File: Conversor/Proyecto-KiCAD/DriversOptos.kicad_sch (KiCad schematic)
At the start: 29 parts, among them U10 ACPL-P480, U11 2ED21834-S06J, U12 2ED21834-S06J, U7 ACPL-P480, U8 ACPL-P480, U9 ACPL-P480

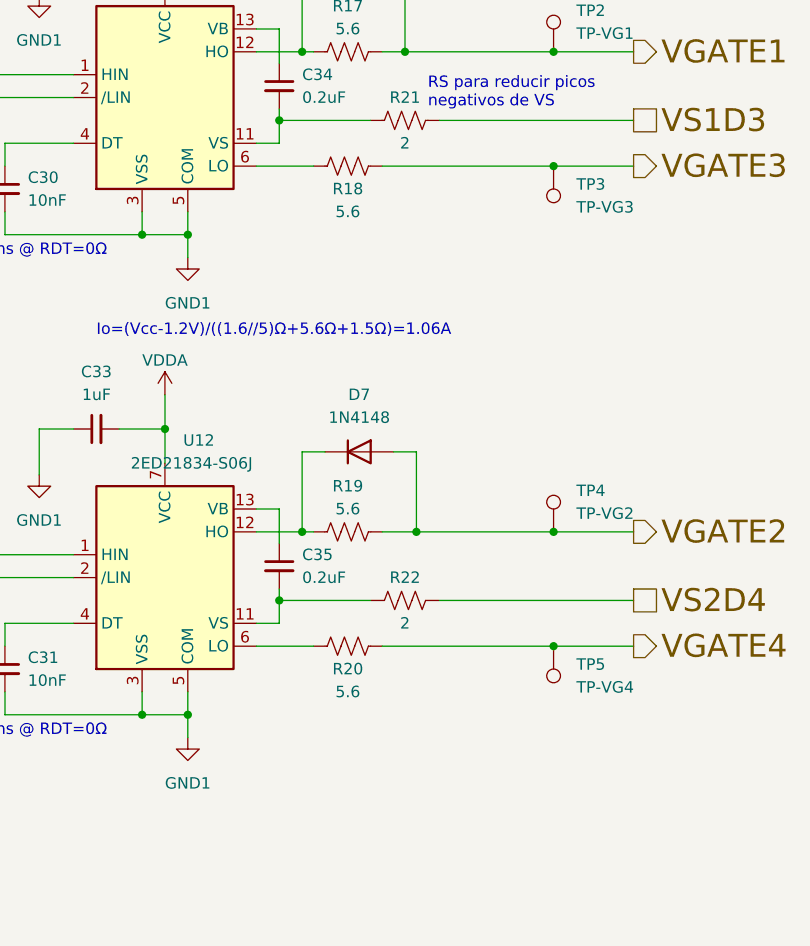
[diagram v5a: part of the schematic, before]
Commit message: Arreglar los primeros dos items marcados por Jorge
- Usar EPWM1A/B y EPWM2A/B para poder usar la función de phase-shift de
los modulos PWM y ahorrarse la sincronización manual
- Agregar diodos de descarga D8 y D9 a la salida de los drivers
- Agregar el Technical Reference Manual del DSP a la bibliografía
(descripción ultra detallada de todas las funciones del DSP)
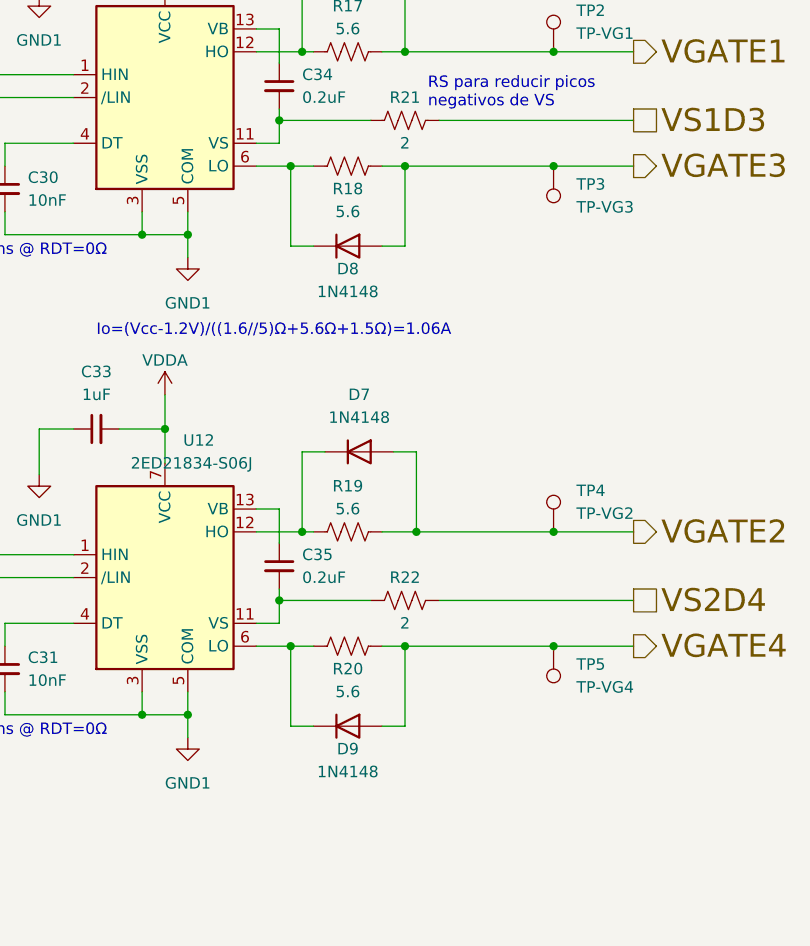
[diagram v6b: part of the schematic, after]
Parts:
- added D8, D9: 1N4148, Diode_THT:D_DO-35_SOD27_P7.62mm_Horizontal, symbol Diode:1N4148
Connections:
- net VGATE3: now also D8.2 (A)
- net VGATE4: now also D9.2 (A)
- net at R20.1, U12.6 (LO): now also D9.1 (K)
- net at R18.1, U11.6 (LO): now also D8.1 (K)
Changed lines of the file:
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@@
 (kicad_sch (version 20211123) (generator eeschema)
   (paper "A4")
+  (junction (at 205.74 129.54) (diameter 0) (color 0 0 0 0)
+  )
   (junction (at 219.71 116.84) (diameter 0) (color 0 0 0 0)
   )
@@
   (junction (at 144.78 46.99) (diameter 0) (color 0 0 0 0)
   )
+  (junction (at 218.44 129.54) (diameter 0) (color 0 0 0 0)
+  )
   (junction (at 234.95 63.5) (diameter 0) (color 0 0 0 0)
   )
+  (junction (at 218.44 76.2) (diameter 0) (color 0 0 0 0)
+  )
   (junction (at 234.95 76.2) (diameter 0) (color 0 0 0 0)
   )
@@
   (junction (at 234.95 116.84) (diameter 0) (color 0 0 0 0)
   )
+  (junction (at 205.74 76.2) (diameter 0) (color 0 0 0 0)
+  )
   (junction (at 144.78 106.68) (diameter 0) (color 0 0 0 0)
   )
@@
     (stroke (width 0) (type default) (color 0 0 0 0))
   )
+  (wire (pts (xy 218.44 129.54) (xy 218.44 138.43))
+    (stroke (width 0) (type default) (color 0 0 0 0))
+  )
   (wire (pts (xy 144.78 67.31) (xy 147.32 67.31))
     (stroke (width 0) (type default) (color 0 0 0 0))
@@
     (stroke (width 0) (type default) (color 0 0 0 0))
   )
-  (wire (pts (xy 201.93 129.54) (xy 208.28 129.54))
+  (wire (pts (xy 201.93 129.54) (xy 205.74 129.54))
     (stroke (width 0) (type default) (color 0 0 0 0))
   )
@@
     (stroke (width 0) (type default) (color 0 0 0 0))
   )
-  (wire (pts (xy 215.9 129.54) (xy 234.95 129.54))
+  (wire (pts (xy 215.9 129.54) (xy 218.44 129.54))
     (stroke (width 0) (type default) (color 0 0 0 0))
   )
@@
     (stroke (width 0) (type default) (color 0 0 0 0))
   )
+  (wire (pts (xy 215.9 85.09) (xy 218.44 85.09))
+    (stroke (width 0) (type default) (color 0 0 0 0))
+  )
   (wire (pts (xy 181.61 127) (xy 173.99 127))
     (stroke (width 0) (type default) (color 0 0 0 0))
@@
     (stroke (width 0) (type default) (color 0 0 0 0))
   )
+  (wire (pts (xy 205.74 129.54) (xy 205.74 138.43))
+    (stroke (width 0) (type default) (color 0 0 0 0))
+  )
   (wire (pts (xy 201.93 116.84) (xy 207.01 116.84))
     (stroke (width 0) (type default) (color 0 0 0 0))
@@
     (stroke (width 0) (type default) (color 0 0 0 0))
   )
+  (wire (pts (xy 205.74 76.2) (xy 205.74 85.09))
+    (stroke (width 0) (type default) (color 0 0 0 0))
+  )
   (wire (pts (xy 144.78 46.99) (xy 147.32 46.99))
     (stroke (width 0) (type default) (color 0 0 0 0))
@@
     (stroke (width 0) (type default) (color 0 0 0 0))
   )
-  (wire (pts (xy 215.9 76.2) (xy 234.95 76.2))
+  (wire (pts (xy 215.9 76.2) (xy 218.44 76.2))
     (stroke (width 0) (type default) (color 0 0 0 0))
   )
@@
     (stroke (width 0) (type default) (color 0 0 0 0))
   )
+  (wire (pts (xy 205.74 76.2) (xy 208.28 76.2))
+    (stroke (width 0) (type default) (color 0 0 0 0))
+  )
+  (wire (pts (xy 218.44 85.09) (xy 218.44 76.2))
+    (stroke (width 0) (type default) (color 0 0 0 0))
+  )
   (wire (pts (xy 181.61 52.07) (xy 177.8 52.07))
     (stroke (width 0) (type default) (color 0 0 0 0))
@@
   )
   (wire (pts (xy 55.88 90.17) (xy 64.77 90.17))
+    (stroke (width 0) (type default) (color 0 0 0 0))
+  )
+  (wire (pts (xy 205.74 129.54) (xy 208.28 129.54))
+    (stroke (width 0) (type default) (color 0 0 0 0))
+  )
+  (wire (pts (xy 208.28 85.09) (xy 205.74 85.09))
+    (stroke (width 0) (type default) (color 0 0 0 0))
+  )
+  (wire (pts (xy 218.44 129.54) (xy 234.95 129.54))
+    (stroke (width 0) (type default) (color 0 0 0 0))
+  )
+  (wire (pts (xy 208.28 138.43) (xy 205.74 138.43))
     (stroke (width 0) (type default) (color 0 0 0 0))
   )
@@
     (stroke (width 0) (type default) (color 0 0 0 0))
   )
+  (wire (pts (xy 218.44 76.2) (xy 234.95 76.2))
+    (stroke (width 0) (type default) (color 0 0 0 0))
+  )
   (wire (pts (xy 113.03 78.74) (xy 113.03 80.01))
     (stroke (width 0) (type default) (color 0 0 0 0))
@@
     (stroke (width 0) (type default) (color 0 0 0 0))
   )
+  (wire (pts (xy 215.9 138.43) (xy 218.44 138.43))
+    (stroke (width 0) (type default) (color 0 0 0 0))
+  )
   (wire (pts (xy 162.56 114.3) (xy 162.56 119.38))
     (stroke (width 0) (type default) (color 0 0 0 0))
@@
     (stroke (width 0) (type default) (color 0 0 0 0))
   )
-  (wire (pts (xy 201.93 76.2) (xy 208.28 76.2))
+  (wire (pts (xy 201.93 76.2) (xy 205.74 76.2))
     (stroke (width 0) (type default) (color 0 0 0 0))
   )
@@
     (pin "1")
   )
+  (symbol (lib_id "Diode:1N4148") (at 212.09 138.43 0) (unit 1)
+    (in_bom yes) (on_board yes)
+    (property "Reference" "D9" (id 0) (at 212.09 140.97 0))
+    (property "Value" "1N4148" (id 1) (at 212.09 143.51 0))
+    (property "Footprint" "Diode_THT:D_DO-35_SOD27_P7.62mm_Horizontal" (id 2) (at 212.09 142.875 0)
+      (effects (font (size 1.27 1.27)) hide)
+    )
+    (property "Datasheet" "https://assets.nexperia.com/documents/data-sheet/1N4148_1N4448.pdf" (id 3) (at 212.09 138.43 0)
+      (effects (font (size 1.27 1.27)) hide)
+    )
+    (pin "1")
+    (pin "2")
+  )
+  (symbol (lib_id "Diode:1N4148") (at 212.09 85.09 0) (unit 1)
+    (in_bom yes) (on_board yes)
+    (property "Reference" "D8" (id 0) (at 212.09 87.63 0))
+    (property "Value" "1N4148" (id 1) (at 212.09 90.17 0))
+    (property "Footprint" "Diode_THT:D_DO-35_SOD27_P7.62mm_Horizontal" (id 2) (at 212.09 89.535 0)
+      (effects (font (size 1.27 1.27)) hide)
+    )
+    (property "Datasheet" "https://assets.nexperia.com/documents/data-sheet/1N4148_1N4448.pdf" (id 3) (at 212.09 85.09 0)
+      (effects (font (size 1.27 1.27)) hide)
+    )
+    (pin "1")
+    (pin "2")
+  )
 )

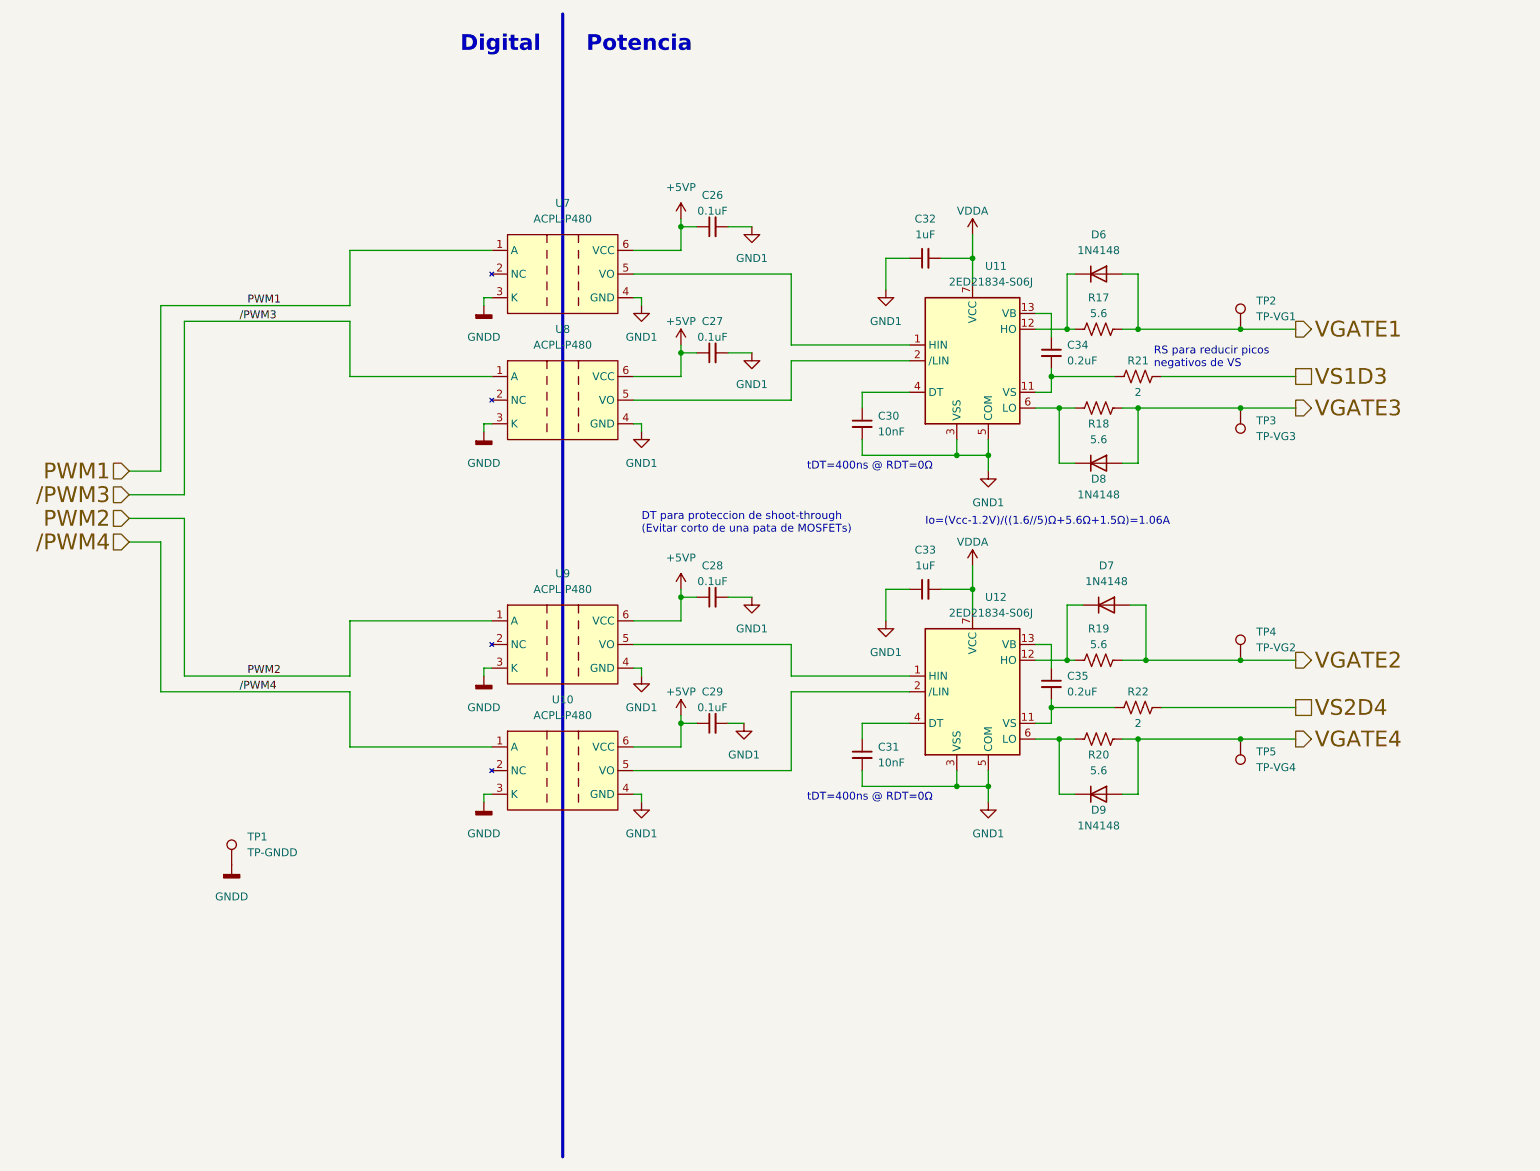
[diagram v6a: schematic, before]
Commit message: Terminar el resto de los cambios de Jorge
- Capacitores electroliticos para el circuito de bootstrap, en paralelo
a los cerámicos
- Cambiar el I2C a 3V3 del lado digital
- Hacer la separacion de linea de datos de I2C del lado digital como en
la nota de aplicación SLYT403A
- Dejar el Vaux del LM5056A con un jumper por si acaso
- Lo mismo con la resistencia de dead-time RDT de los drivers, dejar una
footprint de resistencia SMD para poder cambiarlas de ser necesario
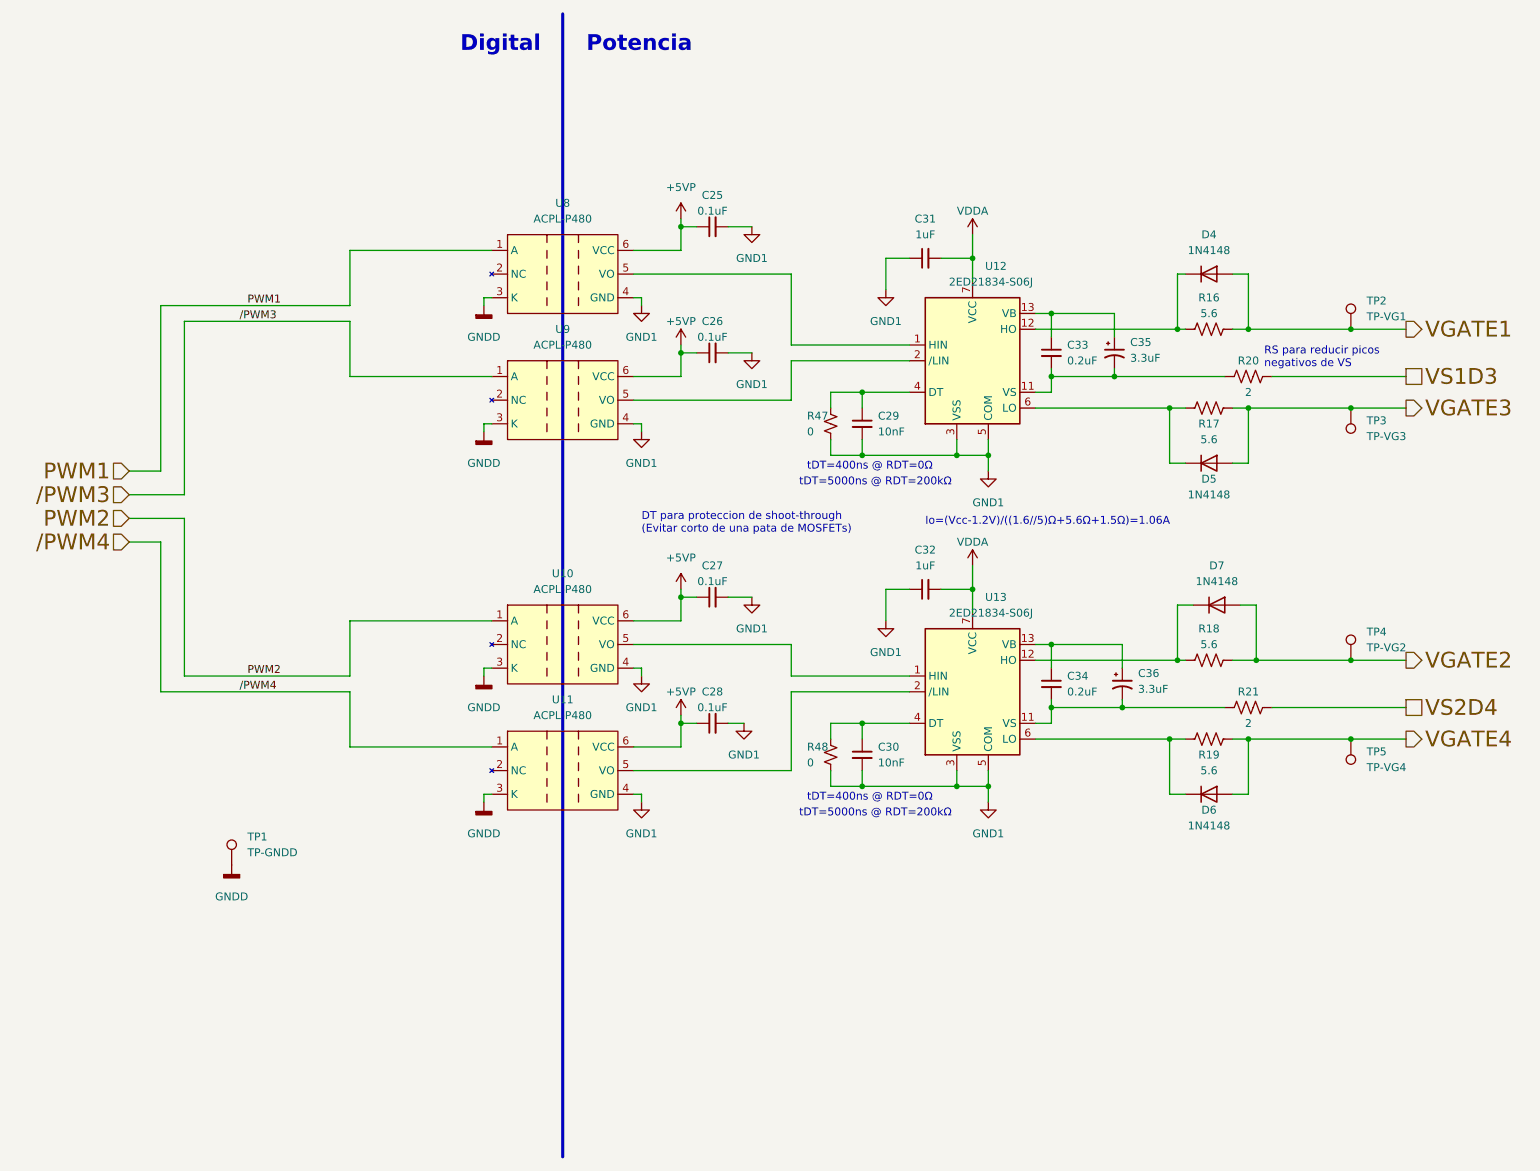
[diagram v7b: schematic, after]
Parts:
- added C35, C36: 3.3uF, Capacitor_THT:CP_Radial_D4.0mm_P2.00mm, symbol Device:C_Polarized_Small_US
- added R47, R48: 0, Resistor_SMD:R_1206_3216Metric_Pad1.30x1.75mm_HandSolder, symbol Device:R_Small_US
- renumbered C26 to C25, C27 to C26, C28 to C27, C29 to C28, C30 to C29, C31 to C30, C32 to C31, C33 to C32, C34 to C33, C35 to C34, D6 to D4, D8 to D5, D9 to D6, R17 to R16, R18 to R17, R19 to R18, R20 to R19, R21 to R20, R22 to R21, U9 to U10, U10 to U11, U11 to U12, U12 to U13, U7 to U8, U8 to U9
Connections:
- net GND1: now also R47.2, R48.2
- net at C30.1, U13.4 (DT): now also R48.1
- net at C34.1, U13.13 (VB): now also C36.1
- net at C34.2, R21.1, U13.11 (VS): now also C36.2
- net at C33.2, R20.1, U12.11 (VS): now also C35.2
- net at C29.1, U12.4 (DT): now also R47.1
- net at C33.1, U12.13 (VB): now also C35.1
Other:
- note added: "tDT=5000ns @ RDT=200kΩ"
- moved on the sheet: D4, D5, D6, D7, R16, R17, R18, R19, R20, R21, TP2, TP3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
